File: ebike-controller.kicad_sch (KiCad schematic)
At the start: 6 parts, among them J5 Conn_01x02, J6 Conn_01x02, J7 Conn_01x02, J8 Conn_01x02, U1 STM32F405RGTx, U2 TCAN330

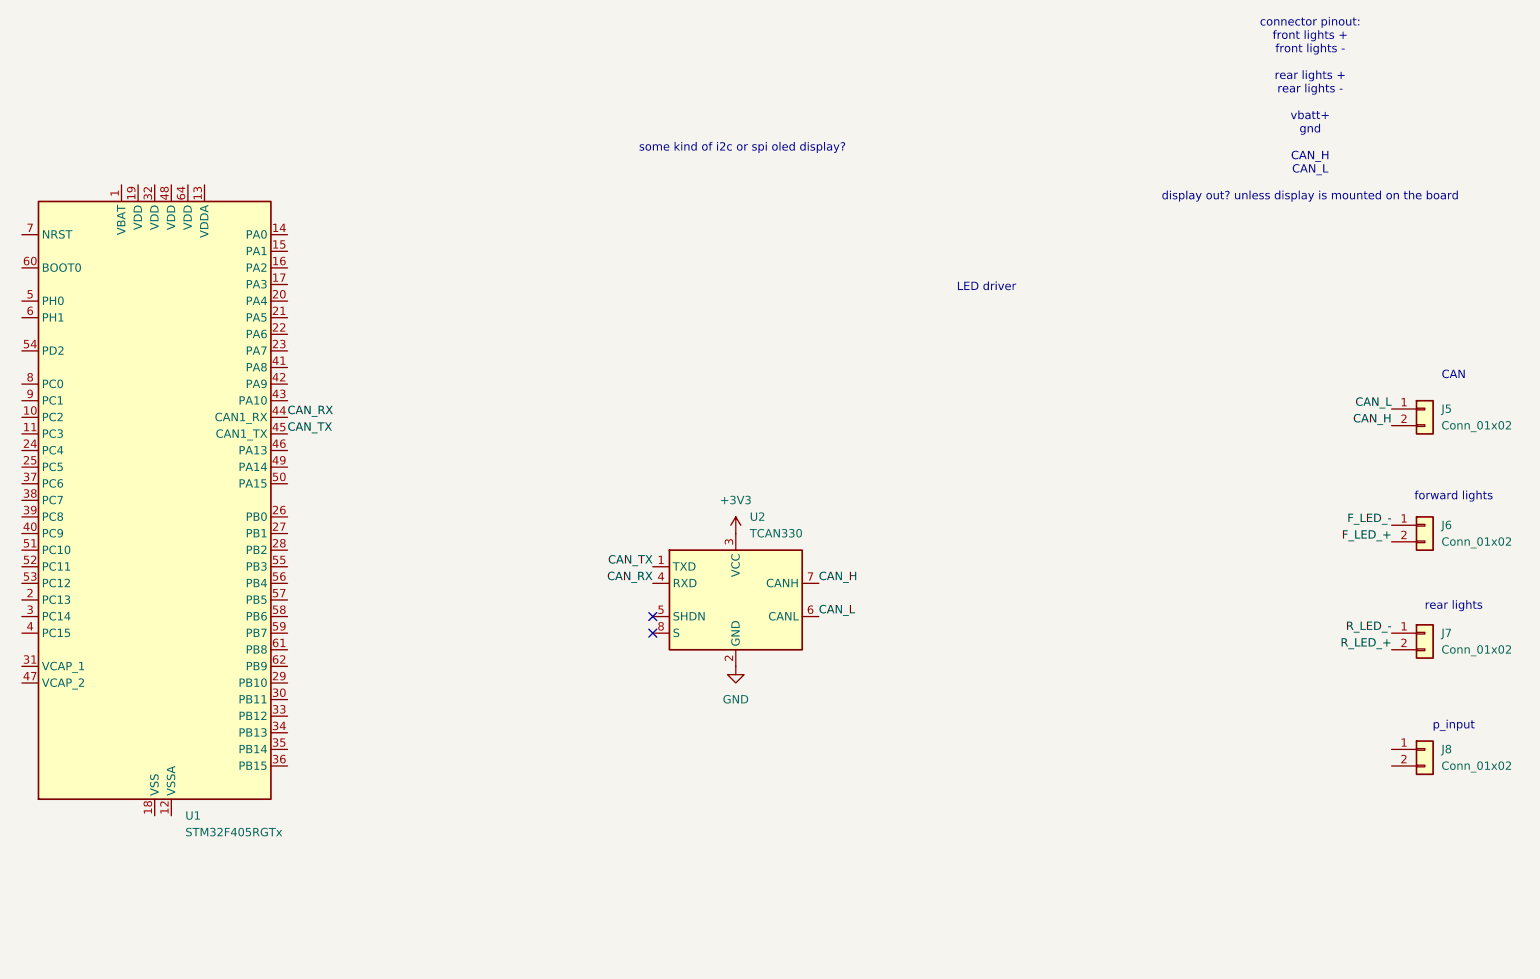
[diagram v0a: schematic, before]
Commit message: improving architecture of schematic
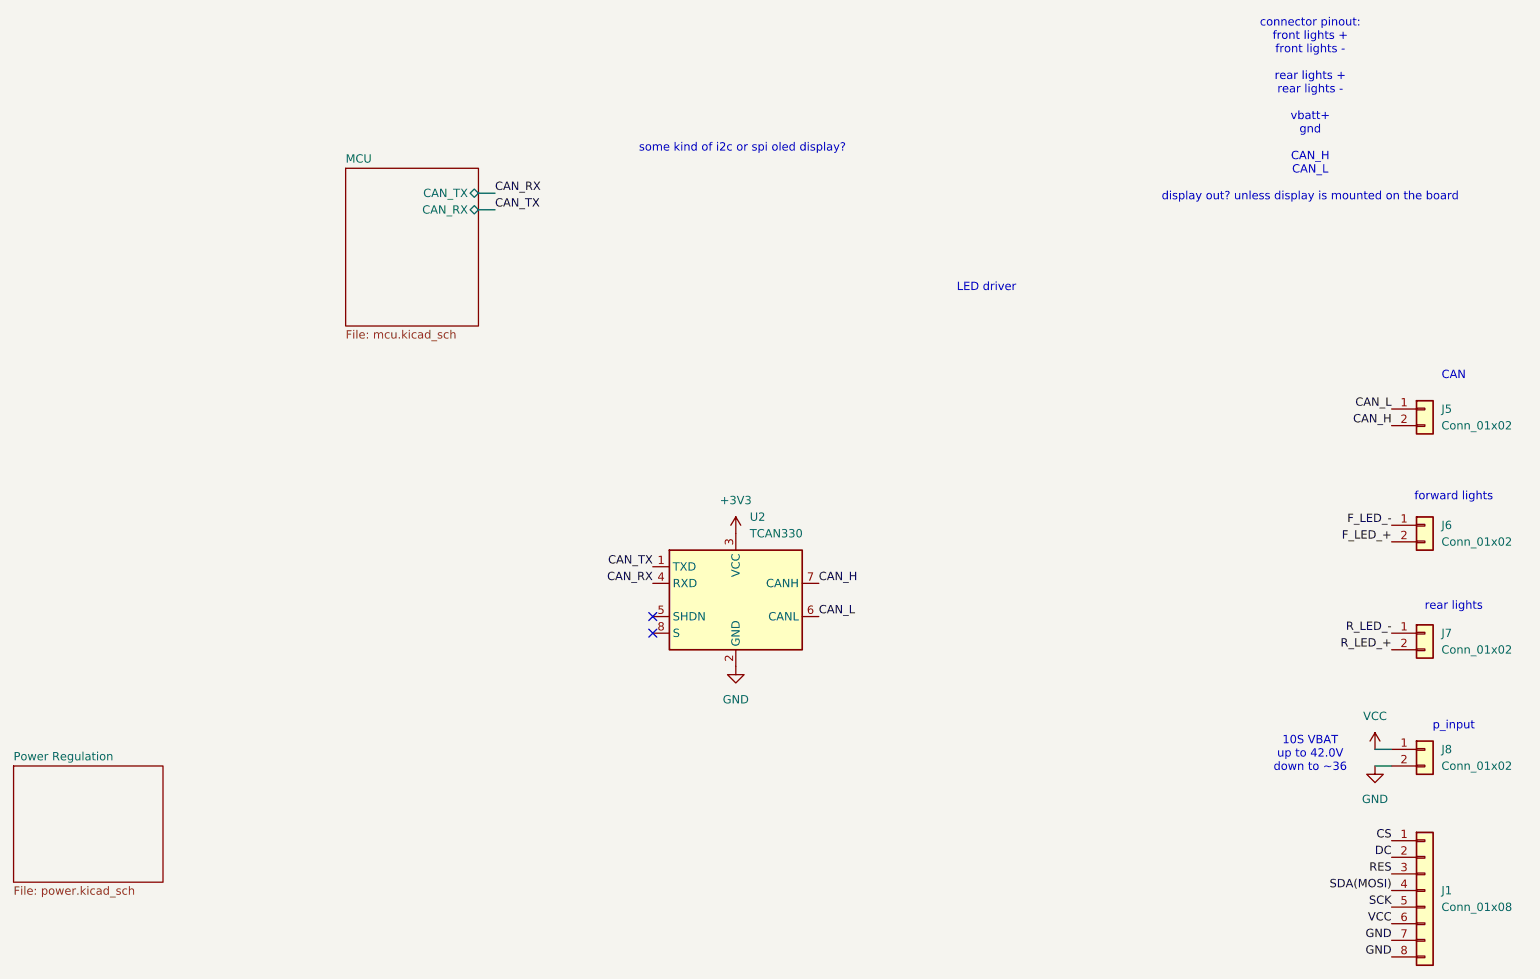
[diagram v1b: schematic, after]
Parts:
- removed U1: STM32F405RGTx, Package_QFP:LQFP-64_10x10mm_P0.5mm, symbol MCU_ST_STM32F4:STM32F405RGTx
- added J1: Conn_01x08, symbol Connector_Generic:Conn_01x08
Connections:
- net GND: now also J8.2 (Pin_2), J1.7 (Pin_7), J1.8 (Pin_8)
- net VCC: now reaches J8.1 (Pin_1)
- net VCC: now also J1.6 (Pin_6)
- new net CS: J1.1 (Pin_1)
- new net DC: J1.2 (Pin_2)
- new net RES: J1.3 (Pin_3)
- new net SCK: J1.5 (Pin_5)
- new net SDA(MOSI): J1.4 (Pin_4)
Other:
- added sheet MCU (mcu.kicad_sch)
- added sheet Power Regulation (power.kicad_sch)
- note added: "10S VBAT up to 42.0V down to ~36"

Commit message: progress checkin
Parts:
- removed J1: Conn_01x08, symbol Connector_Generic:Conn_01x08
- removed J5, J6, J7, J8: Conn_01x02, symbol Connector_Generic:Conn_01x02
- removed U2: TCAN330, Package_SO:SOIC-8_3.9x4.9mm_P1.27mm, symbol Interface_CAN_LIN:TCAN330
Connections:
- no-connect marks 2 -> 0
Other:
- added sheet IO (io.kicad_sch)
- added sheet LED Drivers (led-drivers.kicad_sch)
- sheet MCU ports: added GPIO[0..4], display{7W_SPI}, {CAN}; removed CAN_RX, CAN_TX
- note removed: "10S VBAT up to 42.0V down to ~36"
- note removed: "CAN"
- note removed: "LED driver"
- note removed: "connector pinout: front lights + front lights - rear lights + rear lights - vbatt+ gnd CAN_H CAN_L display out? unless display is mounted on the board"
- note removed: "forward lights"
- note removed: "p_input"
- note removed: "rear lights"
- note removed: "some kind of i2c or spi oled display?"

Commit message: syncing
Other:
- sheet Power Regulation renamed Power
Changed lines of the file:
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@@
 			(color 0 0 0 0)
 		)
-		(property "Sheetname" "Power Regulation"
+		(property "Sheetname" "Power"
 			(at 95.25 81.8384 0)
 			(show_name no)
